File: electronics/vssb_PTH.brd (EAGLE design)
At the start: 50.8 x 56.6 mm, 24 parts, among them IC1 LM1458N, IC2 7805TV, IC3 ATTINY25

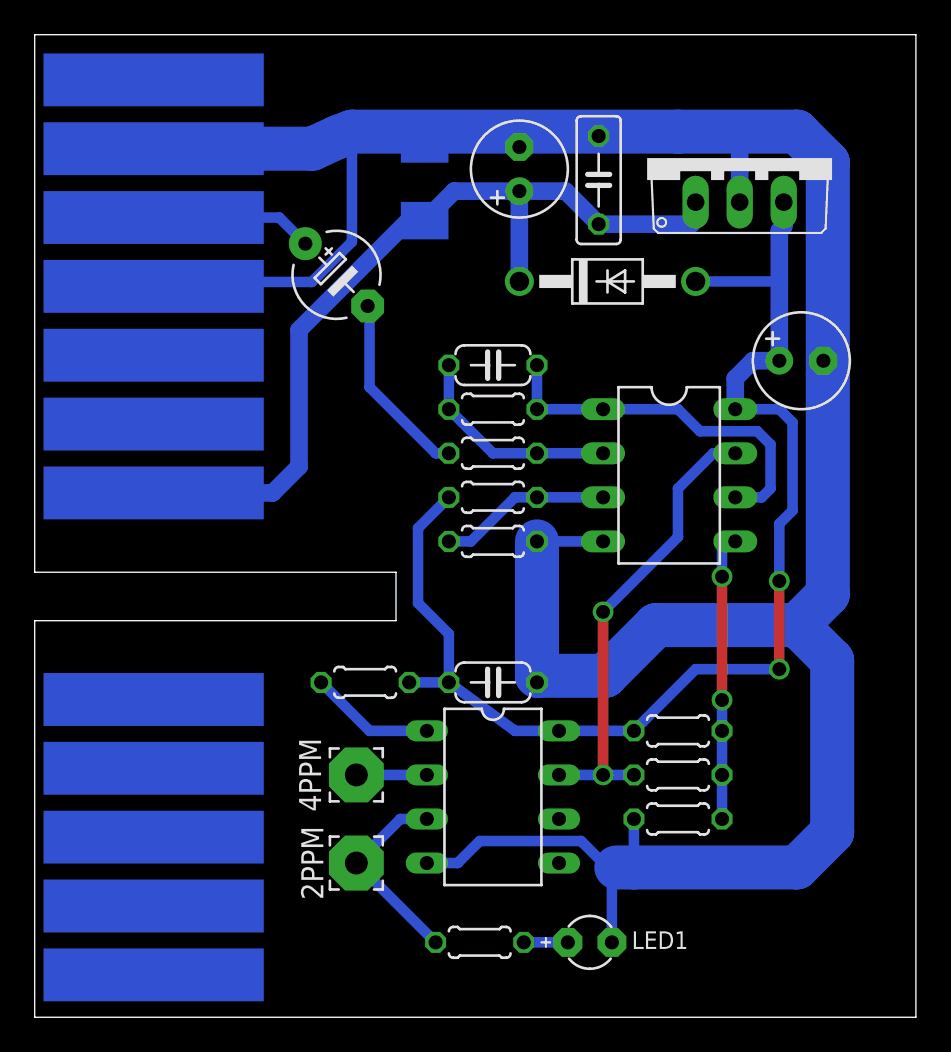
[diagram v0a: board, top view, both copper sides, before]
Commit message: ground plane; minor layout moves for some capacitors and regulator, reroute, shrunk board width
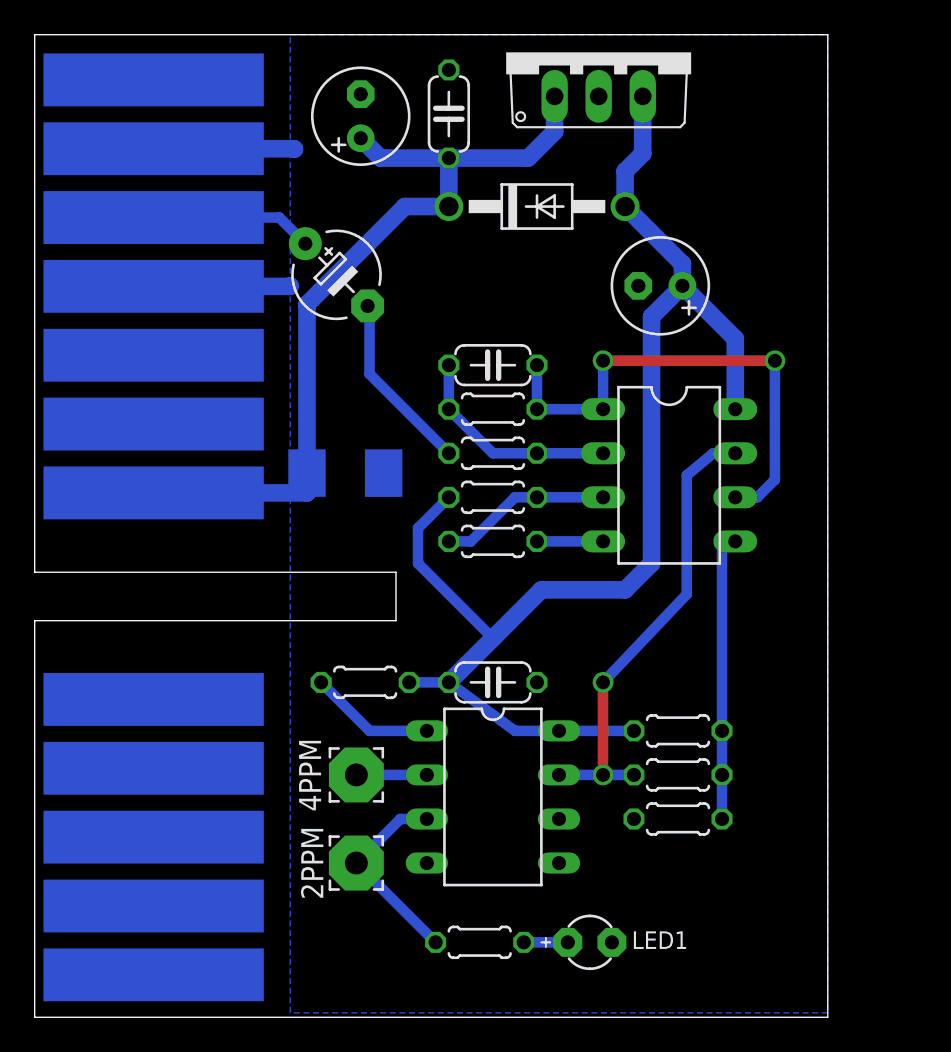
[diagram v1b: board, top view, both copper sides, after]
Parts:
- C21: device rcl:C050-025X075 -> rcl:C050-024X044
- moved D21 17.4 mm to (17.9, 31.4), turned to 180 degrees
- moved IC2 10.2 mm to (32.5, 55.6)
- moved C22 9.64 mm to (18.8, 51.9)
- moved C21 9.44 mm to (23.9, 52.1)
- moved C23 9.20 mm to (36.1, 42.2), turned to 180 degrees
- moved D23 5.93 mm to (29.0, 46.7)
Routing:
- net GND: track 185.6 -> 19.8 mm
- net OUT1: track 21.6 -> 28.6 mm, vias 0 -> 2
- net VCC: track 72.8 -> 76.9 mm, vias 2 -> 0
- net +14V: track 50.2 -> 47.3 mm
- net N$4: vias 2 -> 0
- added copper zone on layer 16, net GND
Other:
- board size 50.8 x 56.6 mm -> 45.7 x 56.6 mm

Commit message: shrunk card edge and board width
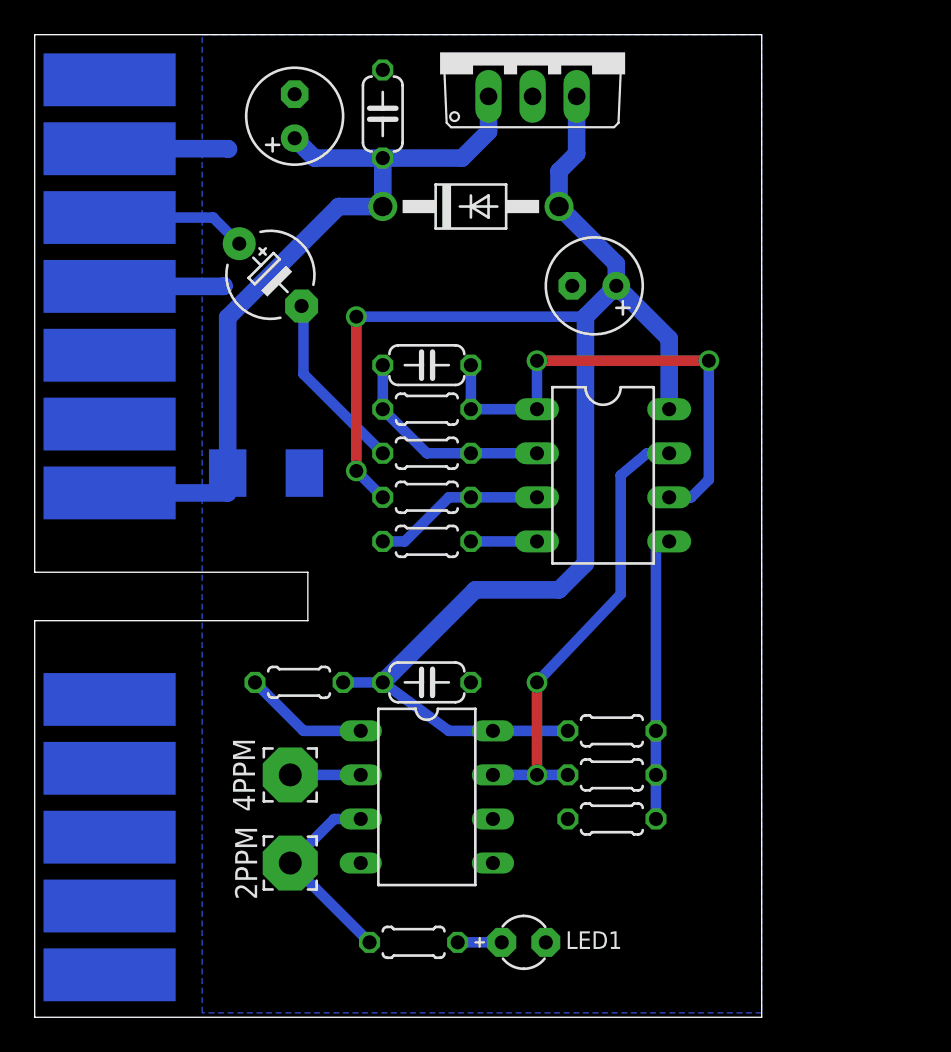
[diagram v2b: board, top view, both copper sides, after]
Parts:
- moved D21 4.57 mm to (13.3, 31.4)
- moved 2PPM 3.81 mm to (14.7, 8.89)
- moved 4PPM 3.81 mm to (14.7, 14.0)
- moved C21 3.81 mm to (20.1, 52.1)
- moved IC1 3.81 mm to (32.8, 31.2)
- moved R15 3.81 mm to (33.3, 16.5)
- moved R16 3.81 mm to (33.3, 11.4)
- moved R17 3.81 mm to (33.3, 14.0)
- moved C11 3.81 mm to (13.6, 42.8)
- moved R41 3.81 mm to (15.2, 19.3)
- moved C12 3.81 mm to (22.6, 37.6)
- moved C22 3.81 mm to (15.0, 51.9)
- moved D23 3.81 mm to (25.1, 46.7)
- moved D41 3.81 mm to (22.6, 19.3)
- moved IC2 3.81 mm to (28.7, 55.6)
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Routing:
- net VCC: track 76.9 -> 90.5 mm, vias 0 -> 2
- net GND: track 19.8 -> 17.3 mm
- net +14V: track 47.3 -> 45.6 mm
- net VSS1: track 9.37 -> 8.10 mm
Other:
- board size 45.7 x 56.6 mm -> 41.9 x 56.6 mm

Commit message: Changed input series cap to 22uF based on experimentation
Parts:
- C11: value 10uF -> 22uF
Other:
- outline, holes or cut-outs redrawn
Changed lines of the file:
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@@
 <layer number="43" name="vRestrict" color="2" fill="10" visible="no" active="yes"/>
 <layer number="44" name="Drills" color="7" fill="1" visible="no" active="yes"/>
-<layer number="45" name="Holes" color="7" fill="1" visible="yes" active="yes"/>
+<layer number="45" name="Holes" color="7" fill="1" visible="no" active="yes"/>
 <layer number="46" name="Milling" color="3" fill="1" visible="no" active="yes"/>
 <layer number="47" name="Measures" color="7" fill="1" visible="no" active="yes"/>
@@
 <layer number="106" name="bPlate" color="7" fill="1" visible="no" active="yes"/>
 <layer number="107" name="Crop" color="7" fill="1" visible="no" active="yes"/>
-<layer number="108" name="tplace-old" color="10" fill="1" visible="yes" active="yes"/>
-<layer number="109" name="ref-old" color="11" fill="1" visible="yes" active="yes"/>
+<layer number="108" name="tplace-old" color="10" fill="1" visible="no" active="yes"/>
+<layer number="109" name="ref-old" color="11" fill="1" visible="no" active="yes"/>
 <layer number="110" name="fp0" color="7" fill="1" visible="no" active="yes"/>
 <layer number="111" name="LPC17xx" color="7" fill="1" visible="no" active="yes"/>
@@
 <layer number="154" name="FabDoc2" color="7" fill="1" visible="no" active="yes"/>
 <layer number="155" name="FabDoc3" color="7" fill="1" visible="no" active="yes"/>
-<layer number="199" name="Contour" color="7" fill="1" visible="yes" active="yes"/>
+<layer number="199" name="Contour" color="7" fill="1" visible="no" active="yes"/>
 <layer number="200" name="200bmp" color="1" fill="10" visible="no" active="yes"/>
 <layer number="201" name="201bmp" color="2" fill="10" visible="no" active="yes"/>
@@
 <wire x1="41.91" y1="56.642" x2="0" y2="56.642" width="0" layer="20"/>
 <wire x1="0" y1="56.642" x2="0" y2="25.654" width="0" layer="20"/>
-<wire x1="0" y1="25.654" x2="15.748" y2="25.654" width="0" layer="20"/>
-<wire x1="15.748" y1="25.654" x2="15.748" y2="22.86" width="0" layer="20"/>
-<wire x1="15.748" y1="22.86" x2="0" y2="22.86" width="0" layer="20"/>
+<wire x1="0" y1="25.654" x2="19.558" y2="25.654" width="0" layer="20"/>
+<wire x1="19.558" y1="25.654" x2="19.558" y2="22.86" width="0" layer="20"/>
+<wire x1="19.558" y1="22.86" x2="0" y2="22.86" width="0" layer="20"/>
 <wire x1="0" y1="22.86" x2="0" y2="0" width="0" layer="20"/>
 </plain>
@@
 <attribute name="VALUE" x="19.177" y="6.3754" size="1.016" layer="27" font="vector" ratio="12"/>
 </element>
-<element name="C11" library="rcl" package="E5-5" value="10uF" x="13.589" y="42.799" smashed="yes" rot="R315">
+<element name="C11" library="rcl" package="E5-5" value="22uF" x="13.589" y="42.799" smashed="yes" rot="R315">
 <attribute name="VALUE" x="14.471615625" y="46.080303125" size="1.016" layer="27" font="vector" ratio="12" rot="R315"/>
 </element>
@@
 </element>
 <element name="4PPM" library="wirepad" package="3,17/1,3" value="" x="14.732" y="13.97" smashed="yes" rot="R90">
-<attribute name="NAME" x="12.7" y="13.97" size="1.27" layer="25" font="vector" ratio="10" rot="R90" align="bottom-center"/>
+<attribute name="NAME" x="12.7" y="13.97" size="1.27" layer="25" font="vector" ratio="12" rot="R90" align="bottom-center"/>
 </element>
 <element name="R41" library="rcl" package="0204/5" value="10k" x="15.24" y="19.304" smashed="yes">
@@
 <wire x1="28.956" y1="27.432" x2="25.146" y2="27.432" width="0.6096" layer="16"/>
 <contactref element="LED1" pad="K"/>
-<polygon width="0.4064" layer="16">
+<polygon width="0.4064" layer="16" isolate="0.3048">
 <vertex x="9.652" y="56.642"/>
 <vertex x="41.91" y="56.642"/>
